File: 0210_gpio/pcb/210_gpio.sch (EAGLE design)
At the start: 24 parts

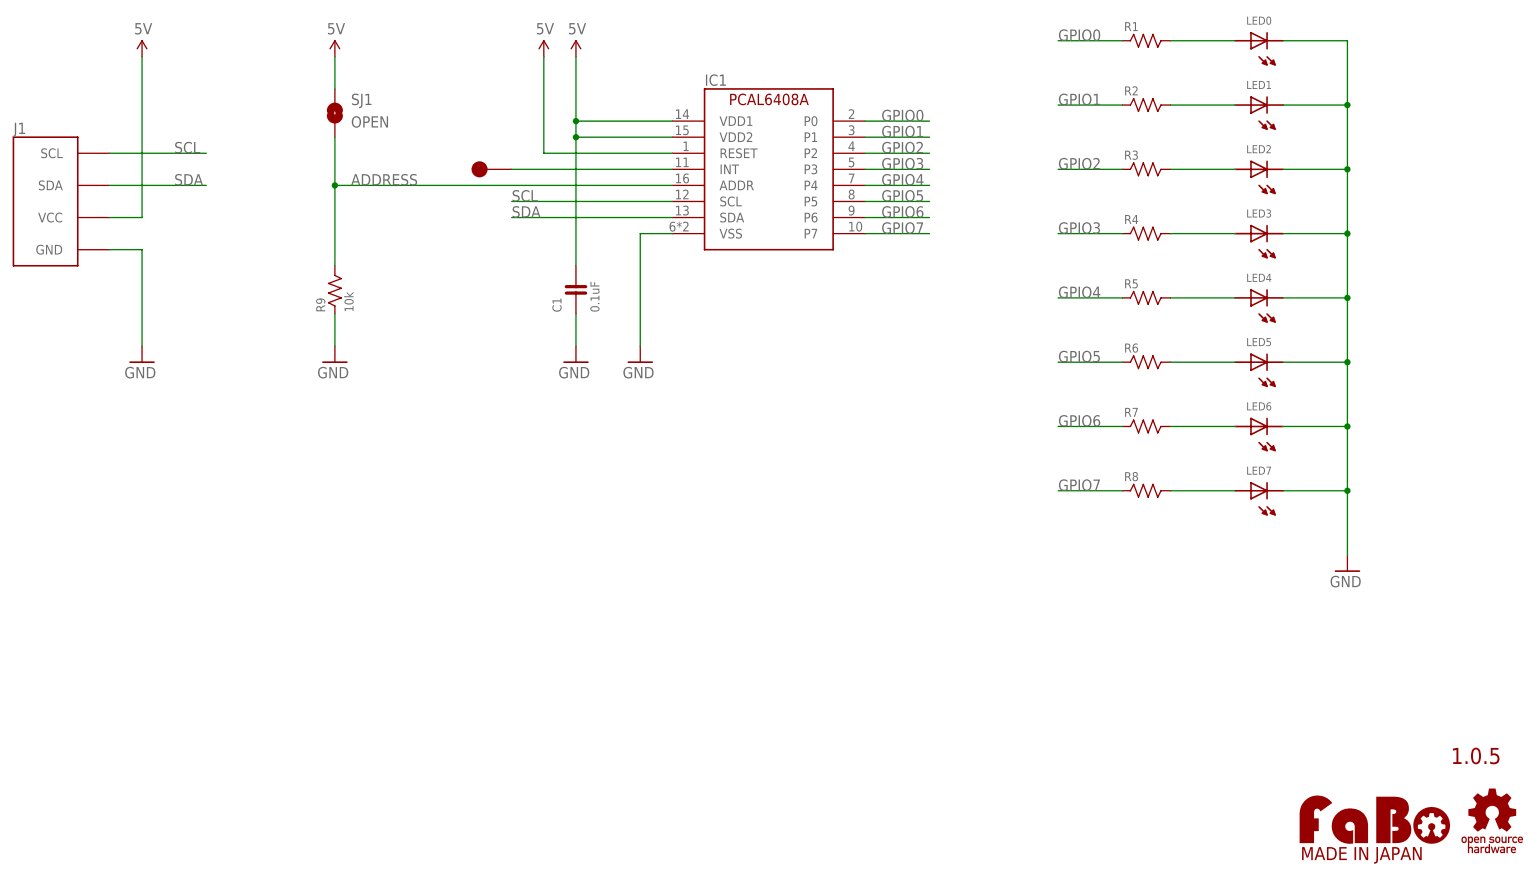
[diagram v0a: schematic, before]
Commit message: GPIO_210_107A
add Reset circuit
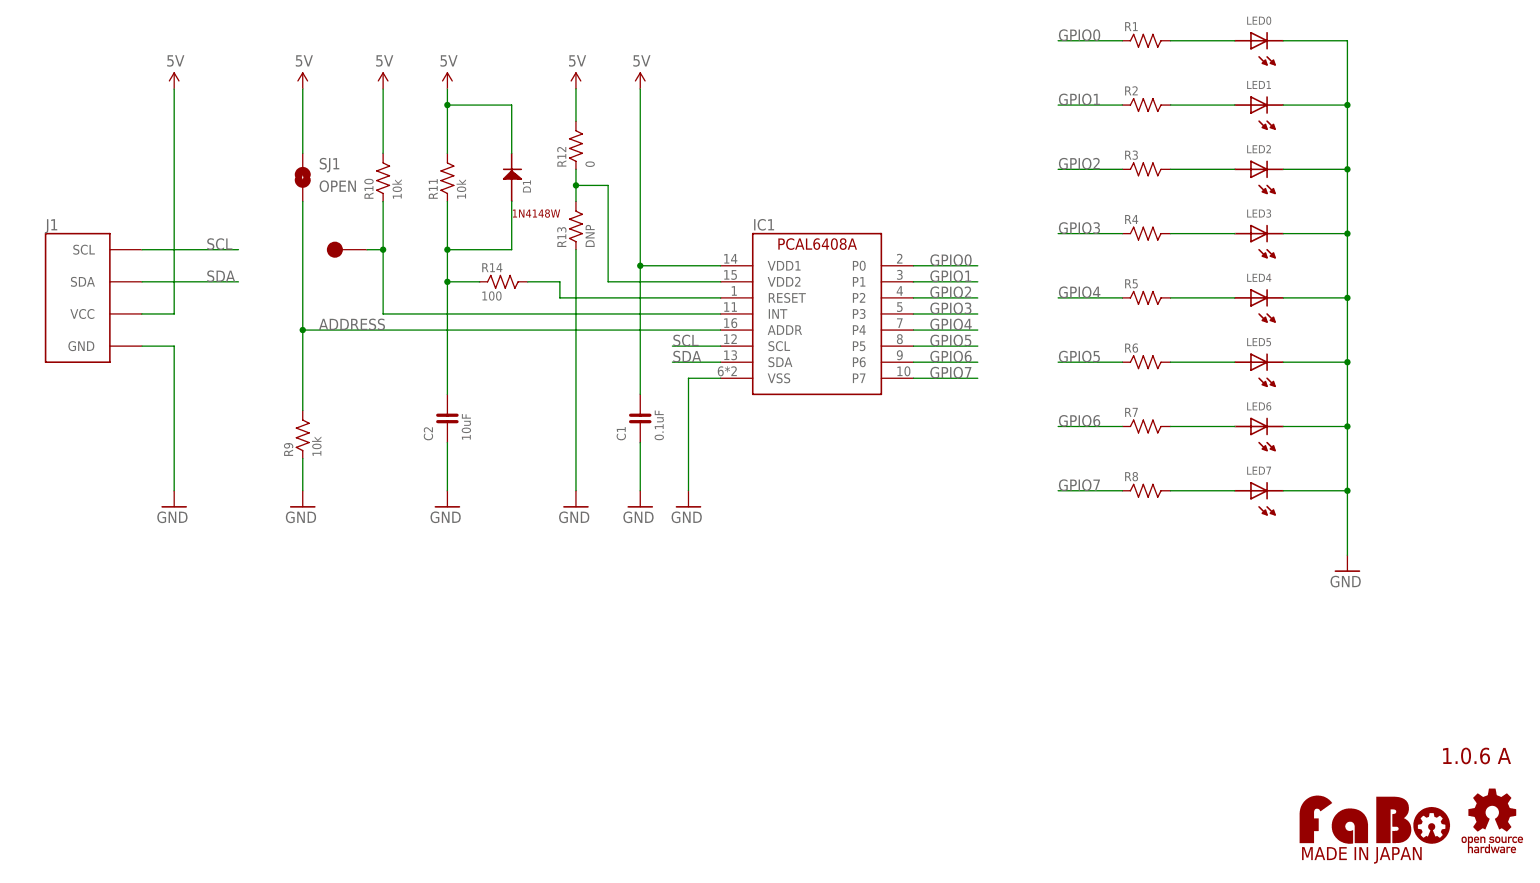
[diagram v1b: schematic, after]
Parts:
- added C2: 10uF, FaBo-Capacitor:CAPACITOR-0805
- added D1: 1N4148, FaBo-Diode:1N4148
- added R10, R11: 10k, FaBo-Resistors:RESISTOR-0603-NARROW
- added R12: 0, FaBo-Resistors:RESISTOR-0603-NARROW
- added R13: DNP, FaBo-Resistors:RESISTOR-0603-NARROW
- added R14: 100, FaBo-Resistors:RESISTOR-0603-NARROW
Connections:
- removed net INT: IC1.INT, TP1.1
- new net N$10: C2.2, D1.ANODE, R11.1, R14.1
- new net N$11: IC1.RESET, R14.2
- new net N$12: IC1.VDD2, R12.1, R13.2
- new net N$9: IC1.INT, R10.1, TP1.1
- net 5V: now also D1.CATHODE, R10.2, R11.2, R12.2; no longer IC1.RESET, IC1.VDD2
- net GND: now also C2.1, R13.1
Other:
- note added: "1.0.6 A"
- note added: "1N4148W"
- note removed: "1.0.5"
- moved on the sheet: C1, IC1, J1, R9, SJ1

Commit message: 210_gpio　ロゴ修正、少しリルート
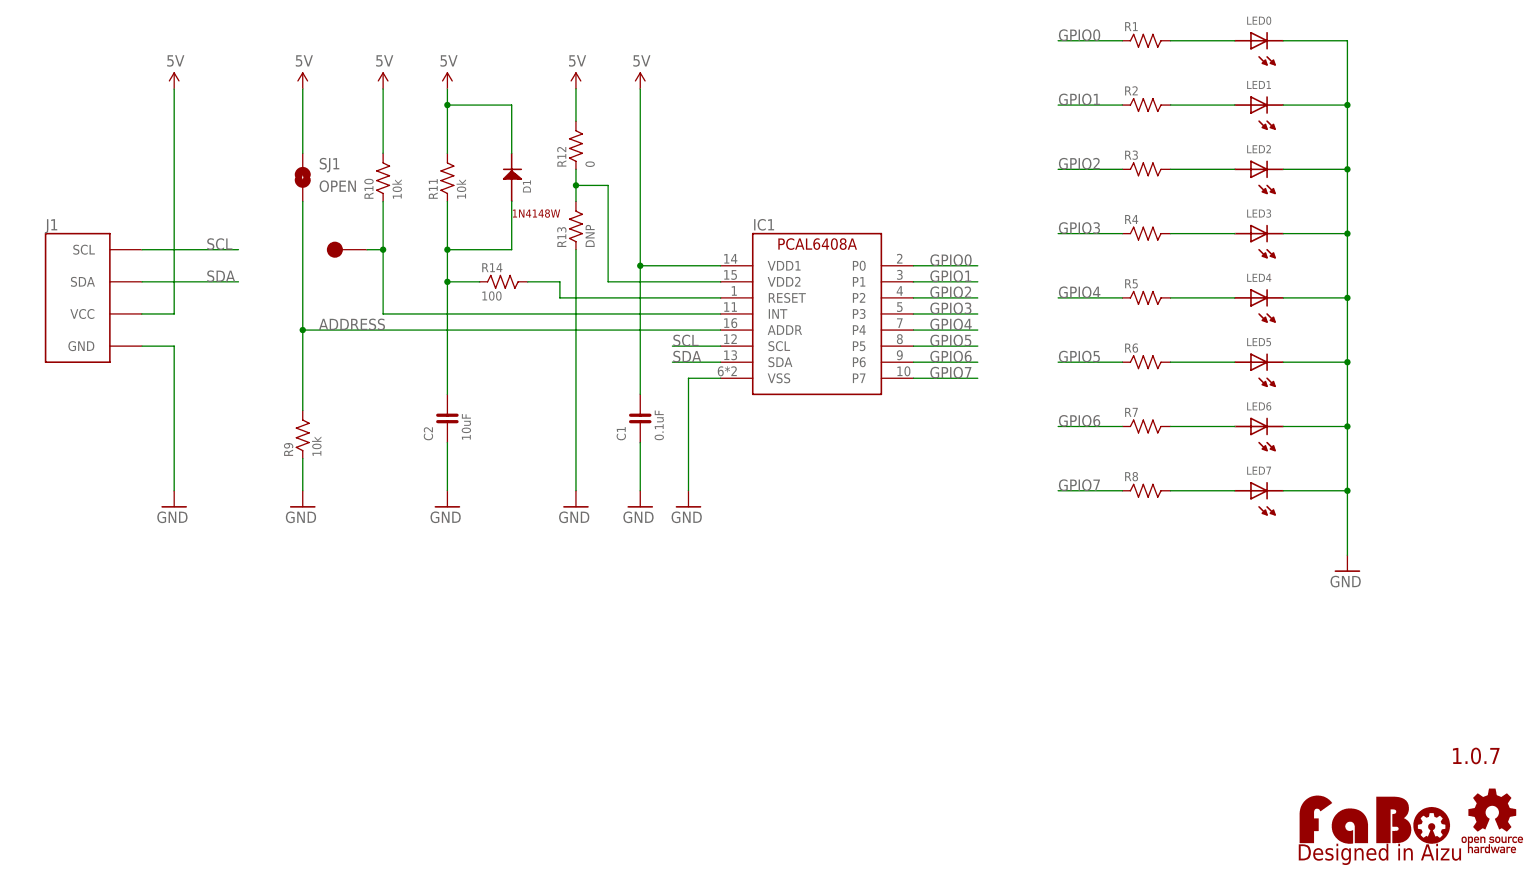
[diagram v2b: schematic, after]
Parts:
- removed U$4: (no value), FaBo-etc:LOGO_FABO-M
- added LOGO1: (no value), component:LOGO_FABO-M
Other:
- note added: "1.0.7"
- note removed: "1.0.6 A"
